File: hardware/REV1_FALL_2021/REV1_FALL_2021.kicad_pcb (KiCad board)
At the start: 2 copper layers, 146 x 133.4 mm, 24 parts, among them J101 Screw_Terminal_01x02, Q101 Q_NMOS_GDS, U1 Teensy3.6_All_Pins, U2 PA16165_Breakout, U201 TPS2113ADRBR, U3 MPL3115A2_Breakout, U301 TPS2113ADRBR, U4 BNO055_Breakout, U5 RFM69HCW_Breakout

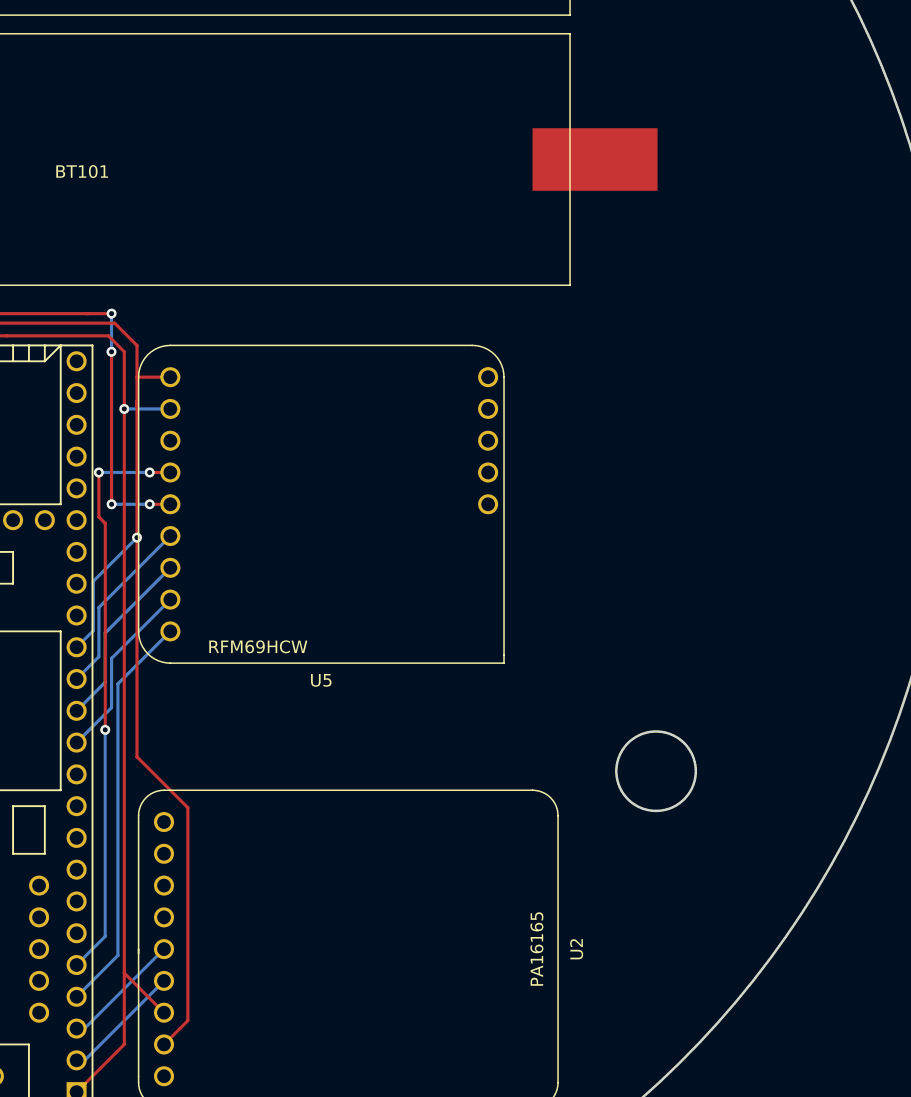
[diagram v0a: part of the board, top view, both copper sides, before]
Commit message: add LEDs to layout
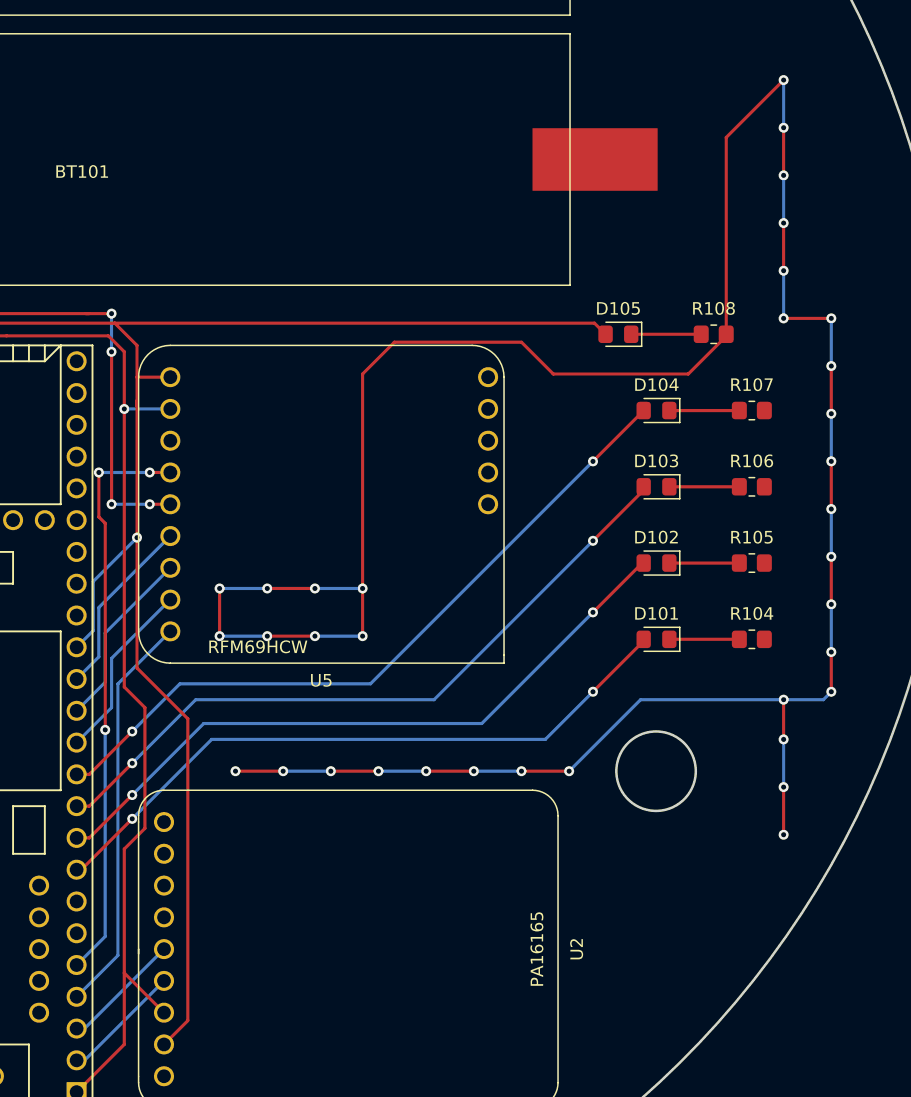
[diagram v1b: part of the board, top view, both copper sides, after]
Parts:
- added D101: LED, LED_SMD:LED_0805_2012Metric_Pad1.15x1.40mm_HandSolder, F.Cu at (149.9, 120.9)
- added D102: LED, LED_SMD:LED_0805_2012Metric_Pad1.15x1.40mm_HandSolder, F.Cu at (149.9, 114.8)
- added D103: LED, LED_SMD:LED_0805_2012Metric_Pad1.15x1.40mm_HandSolder, F.Cu at (149.9, 108.7)
- added D104: LED, LED_SMD:LED_0805_2012Metric_Pad1.15x1.40mm_HandSolder, F.Cu at (149.9, 102.6)
- added D105: LED, LED_SMD:LED_0805_2012Metric_Pad1.15x1.40mm_HandSolder, F.Cu at (146.8, 96.5)
- added R104: R_750, Resistor_SMD:R_0805_2012Metric_Pad1.20x1.40mm_HandSolder, F.Cu at (157.5, 120.9)
- added R105: R_750, Resistor_SMD:R_0805_2012Metric_Pad1.20x1.40mm_HandSolder, F.Cu at (157.5, 114.8)
- added R106: R_750, Resistor_SMD:R_0805_2012Metric_Pad1.20x1.40mm_HandSolder, F.Cu at (157.5, 108.7)
- added R107: R_750, Resistor_SMD:R_0805_2012Metric_Pad1.20x1.40mm_HandSolder, F.Cu at (157.5, 102.6)
- added R108: R_750, Resistor_SMD:R_0805_2012Metric_Pad1.20x1.40mm_HandSolder, F.Cu at (154.4, 96.5)
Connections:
- U1 pad 10: Net-(U1-Pad10) -> /LED_3
- U1 pad 11: Net-(U1-Pad11) -> /LED_4
- U1 pad 8: Net-(U1-Pad8) -> /LED_1
- U1 pad 9: Net-(U1-Pad9) -> /LED_2
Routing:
- net GND: track 232.8 -> 450.3 mm, vias 28 -> 63
- net /LED_4: track 0.00 -> 57.4 mm, vias 0 -> 2
- net /LED_3: track 0.00 -> 56.1 mm, vias 0 -> 2
- net /LED_2: track 0.00 -> 54.4 mm, vias 0 -> 2
- net /LED_1: track 0.00 -> 53.0 mm, vias 0 -> 2
- net /3.3V: track 175.4 -> 215.0 mm
- net Net-(D105-Pad1): track 0.00 -> 5.59 mm
- net Net-(D104-Pad1): track 0.00 -> 5.59 mm
- net Net-(D103-Pad1): track 0.00 -> 5.59 mm
- net Net-(D102-Pad1): track 0.00 -> 5.59 mm
- net Net-(D101-Pad1): track 0.00 -> 5.59 mm

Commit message: tweak battery positions
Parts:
- moved BT102 1.27 mm to (67.9, 59.7)
- moved BT101 1.27 mm to (67.9, 81.3)
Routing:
- net /TPS2113A for E-match/IN2: track 80.9 -> 82.7 mm
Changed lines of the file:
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@@
     (thickness 1.6)
     (drawings 5)
-    (tracks 416)
+    (tracks 417)
     (zones 0)
     (modules 34)
@@
   )
   (setup
-    (last_trace_width 0.25)
+    (last_trace_width 0.762)
     (user_trace_width 0.4318)
     (user_trace_width 0.762)
@@
   )
   (module Olin_Rocketry:MyBatteryHolder_MPD_BH-18650-PC2 (layer F.Cu)
-    (at 67.945 82.55)
+    (at 67.945 81.28)
     (descr "18650 Battery Holder (http://www.memoryprotectiondevices.com/datasheets/BK-18650-PC2-datasheet.pdf)")
     (tags "18650 Battery Holder")
@@
   )
   (module Olin_Rocketry:MyBatteryHolder_MPD_BH-18650-PC2 (layer F.Cu)
-    (at 67.945 60.96)
+    (at 67.945 59.69)
     (descr "18650 Battery Holder (http://www.memoryprotectiondevices.com/datasheets/BK-18650-PC2-datasheet.pdf)")
     (tags "18650 Battery Holder")
@@
   (segment (start 44.9365 102.4675) (end 46.863 102.4675) (width 0.4318) (layer F.Cu) (net 109) (status 800000))
   (segment (start 42.123 99.654) (end 44.9365 102.4675) (width 0.4318) (layer F.Cu) (net 109))
-  (segment (start 62.945 82.55) (end 60.325 82.55) (width 0.762) (layer F.Cu) (net 109) (status C00000))
-  (segment (start 60.325 82.55) (end 56.6 86.275) (width 0.762) (layer F.Cu) (net 109) (status 400000))
   (segment (start 56.6 86.275) (end 56.515 86.275) (width 0.762) (layer F.Cu) (net 109))
   (segment (start 56.515 86.275) (end 49.4665 86.275) (width 0.762) (layer F.Cu) (net 109) (status 800000))
@@
   (segment (start 56.515 99.06) (end 56.515 86.275) (width 0.762) (layer F.Cu) (net 109))
   (segment (start 53.1075 102.4675) (end 56.515 99.06) (width 0.762) (layer F.Cu) (net 109))
-  (segment (start 62.945 82.55) (end 60.325 82.55) (width 0.762) (layer F.Cu) (net 109) (status C00000))
-  (segment (start 60.325 82.55) (end 54.6735 76.8985) (width 0.762) (layer F.Cu) (net 109) (status 400000))
-  (segment (start 54.6735 76.8985) (end 46.9105 76.8985) (width 0.762) (layer F.Cu) (net 109) (status 800000))
+  (segment (start 54.6735 76.8985) (end 54.61 76.8985) (width 0.762) (layer F.Cu) (net 109))
+  (segment (start 54.61 76.8985) (end 46.9105 76.8985) (width 0.762) (layer F.Cu) (net 109) (status 800000))
+  (segment (start 54.61 76.8985) (end 58.5635 76.8985) (width 0.762) (layer F.Cu) (net 109))
+  (segment (start 58.5635 76.8985) (end 62.945 81.28) (width 0.762) (layer F.Cu) (net 109) (status 800000))
+  (segment (start 56.515 86.275) (end 57.95 86.275) (width 0.762) (layer F.Cu) (net 109))
+  (segment (start 57.95 86.275) (end 62.945 81.28) (width 0.762) (layer F.Cu) (net 109) (status 800000))
   (segment (start 43.4265 82.9975) (end 43.4265 83.7005) (width 0.4318) (layer F.Cu) (net 110) (status 400000))
   (segment (start 40.852 86.275) (end 38.0365 86.275) (width 0.4318) (layer F.Cu) (net 110) (status 800000))
@@
   (segment (start 37.9945 102.4675) (end 36.068 102.4675) (width 0.4318) (layer F.Cu) (net 110) (status 800000))
   (segment (start 40.823 99.639) (end 37.9945 102.4675) (width 0.4318) (layer F.Cu) (net 110))
-  (segment (start 62.945 60.96) (end 50.165 60.96) (width 0.762) (layer F.Cu) (net 110) (status 400000))
+  (segment (start 64.215 59.69) (end 51.435 59.69) (width 0.762) (layer F.Cu) (net 110))
   (segment (start 38.0365 73.0885) (end 38.0365 83.82) (width 0.762) (layer F.Cu) (net 110))
   (segment (start 38.0365 83.82) (end 38.0365 86.275) (width 0.762) (layer F.Cu) (net 110) (status 800000))
-  (segment (start 50.165 60.96) (end 38.0365 73.0885) (width 0.762) (layer F.Cu) (net 110))
+  (segment (start 51.435 59.69) (end 38.0365 73.0885) (width 0.762) (layer F.Cu) (net 110))
   (segment (start 38.0365 83.82) (end 38.0365 83.8835) (width 0.762) (layer F.Cu) (net 110))
   (segment (start 31.115 97.3875) (end 36.2165 102.489) (width 0.762) (layer F.Cu) (net 110) (status 800000))

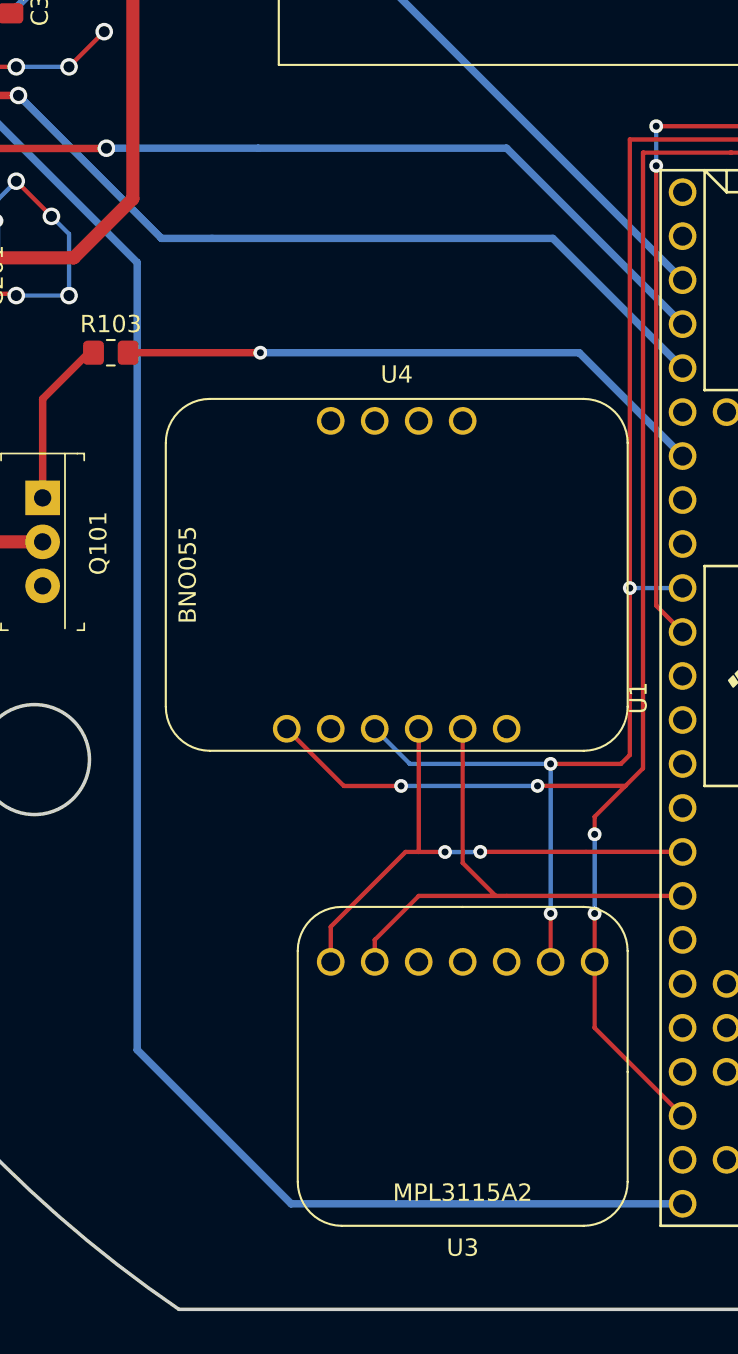
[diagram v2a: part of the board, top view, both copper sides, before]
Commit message: add decoupling capacitor on Teensy VIN pin
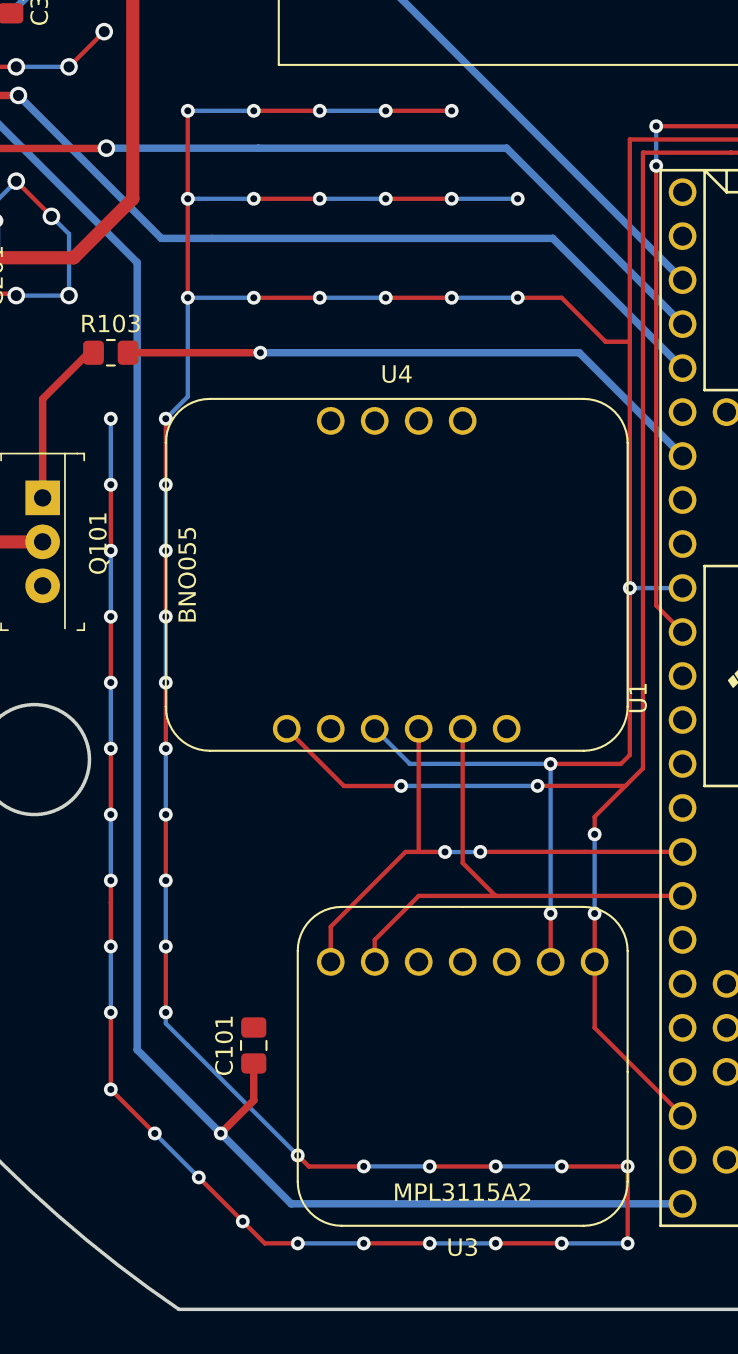
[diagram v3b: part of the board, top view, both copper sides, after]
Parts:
- added C101: C_0.1u, Capacitor_SMD:C_0805_2012Metric_Pad1.18x1.45mm_HandSolder, F.Cu at (63.5, 148.0)
- C203, C303: value C -> C_0.1u
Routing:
- net GND: track 450.3 -> 671.2 mm, vias 63 -> 116
- net /V_TEENSY: track 117.8 -> 122.6 mm, vias 2 -> 3

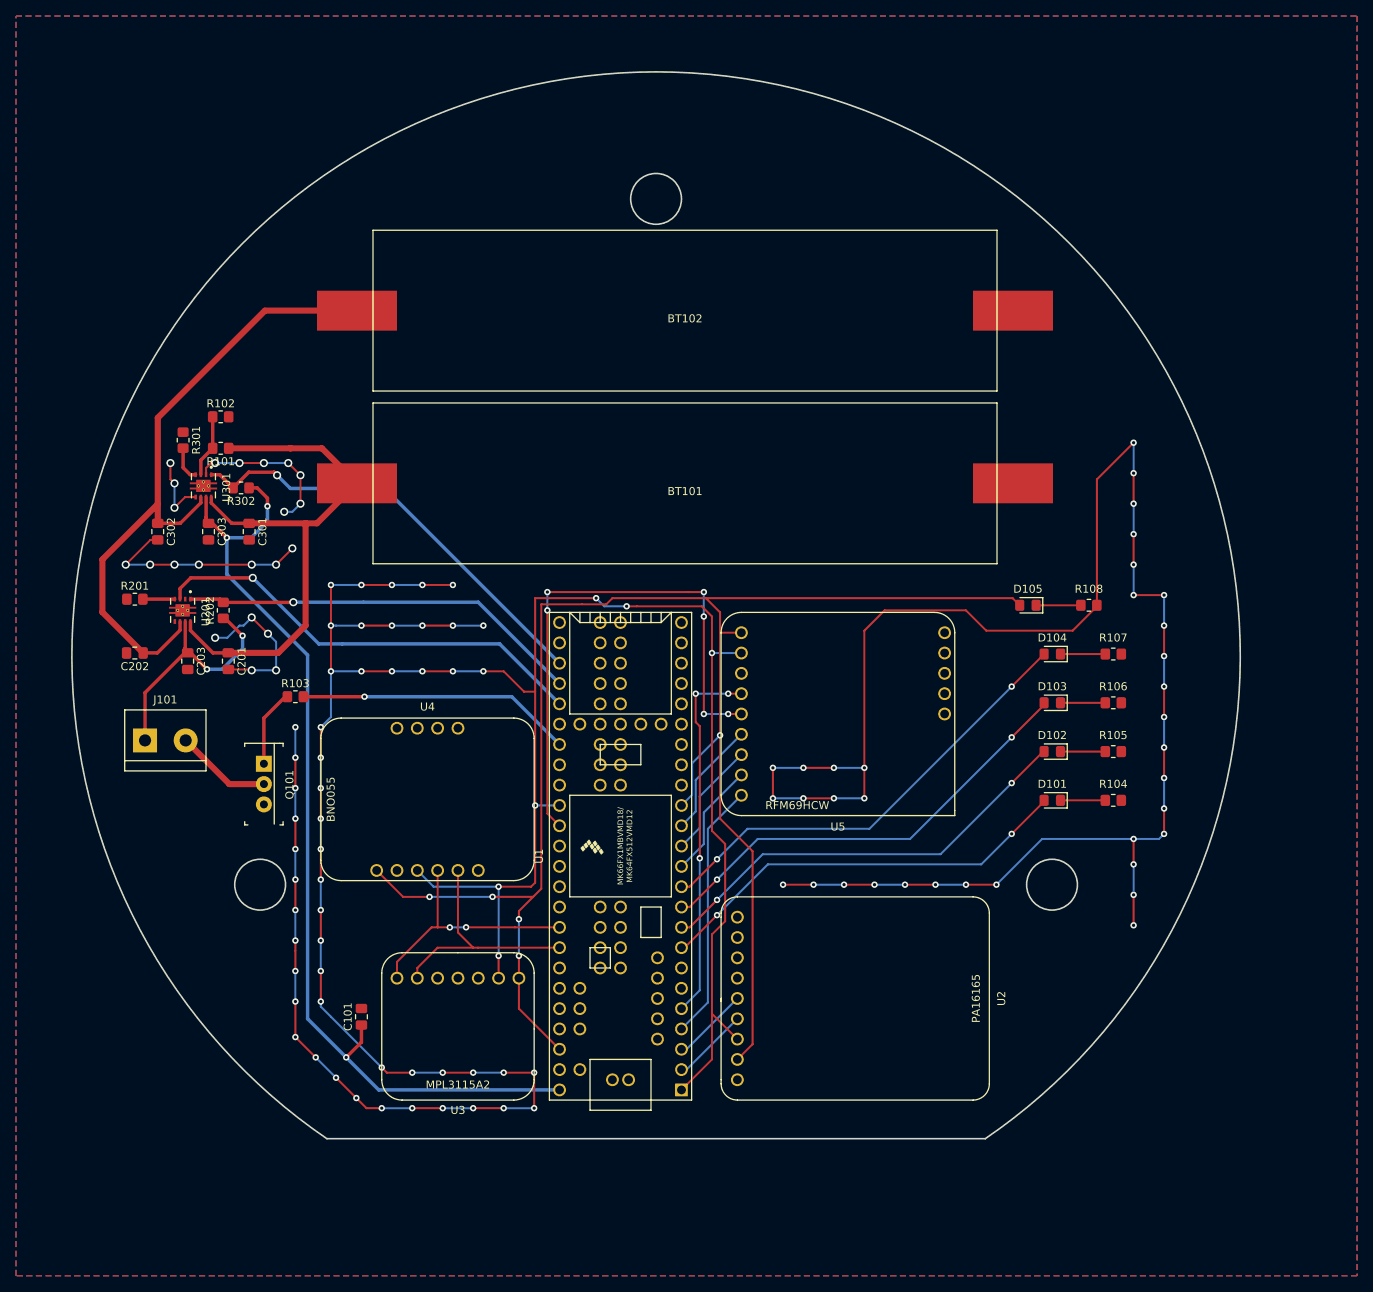
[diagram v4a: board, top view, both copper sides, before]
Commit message: Add second e-match
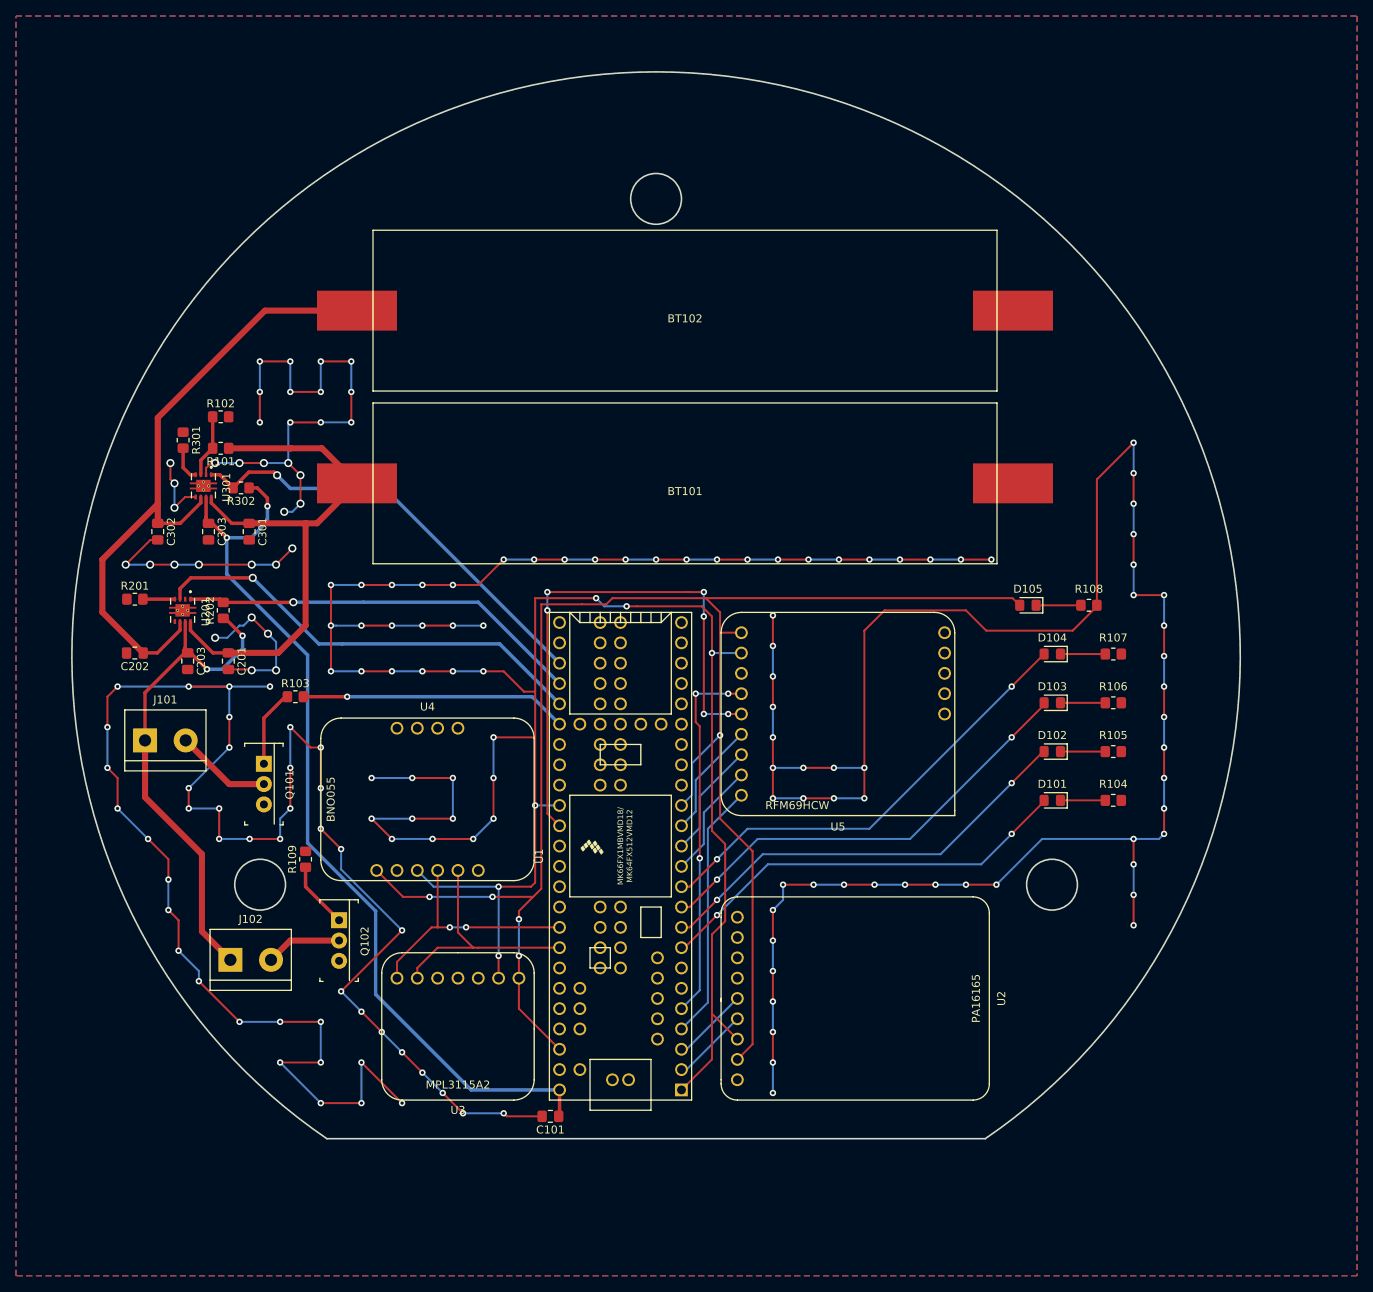
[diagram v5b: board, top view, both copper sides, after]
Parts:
- added J102: Screw_Terminal_01x02, TerminalBlock:TerminalBlock_bornier-2_P5.08mm, F.Cu at (47.1, 140.8)
- added Q102: Q_NMOS_GDS, footprints:TO-220-3, F.Cu at (60.7, 135.9)
- added R109: R_10k, Resistor_SMD:R_0805_2012Metric_Pad1.20x1.40mm_HandSolder, F.Cu at (56.5, 128.3)
- R102: value R_5k -> R_4.7k
- moved C101 26.7 mm to (87.1, 160.4), turned to 180 degrees
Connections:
- R103 pad 2: /E-MATCH_TRIGGER -> /E-MATCH_TRIGGER_1
- U1 pad 35: Net-(U1-Pad35) -> /E-MATCH_TRIGGER_1
- U1 pad 36: /E-MATCH_TRIGGER -> /E-MATCH_TRIGGER_2
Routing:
- net GND: track 671.2 -> 981.1 mm, vias 116 -> 178
- net /E-MATCH_TRIGGER: track 34.5 -> 0.00 mm, vias 1 -> 0
- net /E-MATCH_TRIGGER_1: track 0.00 -> 33.4 mm, vias 0 -> 1
- net /V_EMATCH: track 31.4 -> 63.3 mm
- net Net-(J102-Pad2): track 0.00 -> 9.51 mm
- net Net-(Q102-Pad1): track 0.00 -> 8.36 mm
- net /V_TEENSY: track 122.6 -> 114.4 mm, vias 3 -> 2
